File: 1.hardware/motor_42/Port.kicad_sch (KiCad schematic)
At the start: 0 parts

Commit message: 중간 저장
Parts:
- added J1, J2: Conn_01x06, symbol Connector_Generic:Conn_01x06
- added R11: 120/0.1w, symbol Device:R_Small_US
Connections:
- new net CAN_H: R11.2
- new net GND: J1.5 (Pin_5), J1.6 (Pin_6), J2.5 (Pin_5), J2.6 (Pin_6)
- new net VCC_IN: J1.1 (Pin_1), J1.2 (Pin_2), J2.1 (Pin_1), J2.2 (Pin_2)

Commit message: 살짝 변경
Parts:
- added J3: Conn_01x03, symbol Connector_Generic:Conn_01x03
- added JP2: SolderJumper_2_Open, Jumper:SolderJumper-2_P1.3mm_Open_RoundedPad1.0x1.5mm, symbol Jumper:SolderJumper_2_Open
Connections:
- net CAN_H: now also J1.3 (Pin_3), J2.3 (Pin_3)
- net CAN_L: now also J1.4 (Pin_4), J2.4 (Pin_4), JP2.2 (B)
- net at R11.1: now also JP2.1 (A)

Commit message: 중간 저장
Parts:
- added J4: Conn_01x05, symbol Connector_Generic:Conn_01x05
- added J5: Conn_01x06, symbol Connector_Generic:Conn_01x06
- added SW1, SW2: SW_Push, symbol Switch:SW_Push
- added U5: SN65HVD232, Package_SO:SOIC-8_3.9x4.9mm_P1.27mm, symbol Interface_CAN_LIN:SN65HVD232
- J1: value Conn_01x06 -> CAN_IN
- J2: value Conn_01x06 -> CAN_OUT
- J3: value Conn_01x03 -> DEBUG
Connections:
- net CAN_H: now also U5.7 (CANH)
- net CAN_L: now also U5.6 (CANL)
- net GND: now also J3.3 (Pin_3), J4.3 (Pin_3), J5.2 (Pin_2), SW1.2, SW2.2, U5.2 (GND)
- net SWDIO: now reaches J3.1 (Pin_1)
- net SWCLK: now reaches J3.2 (Pin_2)
- new net 3V3: J5.1 (Pin_1), U5.3 (VCC)
- new net ADC_ENC: J4.5 (Pin_5)
- new net ADC_VREF_2V5: J4.4 (Pin_4)
- new net BTN1: SW1.1
- new net BTN2: SW2.1
- new net CAN_RX: U5.4 (R)
- new net CAN_TX: U5.1 (D)
- new net MT6816_CSN: J5.6 (Pin_6)
- new net SPI1_CLK: J5.3 (Pin_3)
- new net SPI1_MISO: J5.5 (Pin_5)
- new net SPI1_MOSI: J5.4 (Pin_4)
- new net UART1_RX: J4.1 (Pin_1)
- new net UART1_TX: J4.2 (Pin_2)
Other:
- moved on the sheet: J3, JP2, R11

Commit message: 중간 저장
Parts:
- added J6: Conn_01x03, symbol Connector_Generic:Conn_01x03
- SW1, SW2: footprint (none) -> mylib:TSB008A2530A
- renumbered J4 to J1, J3 to J2, J1 to J3, J2 to J4, JP2 to JP1, R11 to R18, U5 to U3
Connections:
- net GND: now also J6.3 (Pin_3)
- new net ESP_RX0: J6.1 (Pin_1)
- new net ESP_TX0: J6.2 (Pin_2)
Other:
- moved on the sheet: J1, J2, J3, J4, J5, JP1, R18, SW1, SW2, U3

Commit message: 회로도 대충 완성
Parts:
- removed SW1, SW2: SW_Push, mylib:TSB008A2530A, symbol Switch:SW_Push
- added D4: PRTR5V0U2X, Package_TO_SOT_SMD:SOT-143, symbol Power_Protection:PRTR5V0U2X
- added J11, J12: Conn_01x02, symbol Connector_Generic:Conn_01x02
- added J3: USB_C, Connector_USB:USB_C_Receptacle_HRO_TYPE-C-31-M-12, symbol USB-C-USB-2.0-cache:Connector_USB_C_Receptacle_USB2.0
- added J9: DEBUG, symbol Connector_Generic:Conn_01x03
- added JP2, JP3, JP4, JP5: SolderJumper_3_Bridged123, Jumper:SolderJumper-3_P1.3mm_Bridged123_RoundedPad1.0x1.5mm, symbol Jumper:SolderJumper_3_Bridged123
- added R24: NC_4.7K, Resistor_SMD:R_0402_1005Metric, symbol Device:R_Small_US
- added R25: 4.7K, Resistor_SMD:R_0402_1005Metric, symbol Device:R_Small_US
- added R39: 4.7k/0.063w, Resistor_SMD:R_0402_1005Metric, symbol Device:R_Small_US
- renumbered J5 to J2, J2 to J4, J3 to J5, J4 to J6, J6 to J7, R18 to R26
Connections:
- net GND: now also D4.1 (GND), J3.A1 (GND), J3.A12 (GND), J3.B1 (GND), J3.B12 (GND), J3.S1 (SHIELD), J9.3 (Pin_3), R25.2
- new net: J3.A5 (CC1), J3.B5 (CC2), R24.2, R25.1
- new net 5V: J9.1 (Pin_1), R39.1
- new net OUT_A+: J11.1 (Pin_1), JP2.1 (A), JP2.2 (C), JP2.3 (B)
- new net OUT_A-: J11.2 (Pin_2), JP3.1 (A), JP3.2 (C), JP3.3 (B)
- new net OUT_B+: J12.1 (Pin_1), JP4.1 (A), JP4.2 (C), JP4.3 (B)
- new net OUT_B-: J12.2 (Pin_2), JP5.1 (A), JP5.2 (C), JP5.3 (B)
- new net USB_DM: D4.3 (I/O2), J3.A7 (D-), J3.B7 (D-)
- new net USB_DP: D4.2 (I/O1), J3.A6 (D+), J3.B6 (D+)
- new net VBUS: D4.4 (VCC), J3.A4 (VBUS), J3.A9 (VBUS), J3.B4 (VBUS), J3.B9 (VBUS), R24.1
- new net WS2812_SIGNAL: J9.2 (Pin_2), R39.2
- no-connect marks 0 -> 2
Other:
- note added: "USB"

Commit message: 수정
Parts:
- J1: value Conn_01x05 -> PC_CONN; footprint (none) -> Connector_JST:JST_SH_SM05B-SRSS-TB_1x05-1MP_P1.00mm_Horizontal
- J11, J12: value Conn_01x02 -> WAGO_2060
- J2: value Conn_01x06 -> MT6816_CONN; footprint (none) -> Connector_JST:JST_SH_SM05B-SRSS-TB_1x05-1MP_P1.00mm_Horizontal
- J4: footprint (none) -> Connector_JST:JST_SH_SM03B-SRSS-TB_1x03-1MP_P1.00mm_Horizontal
- J5, J6: footprint (none) -> Connector_JST:JST_SH_SM06B-SRSS-TB_1x06-1MP_P1.00mm_Horizontal
- J7: value Conn_01x03 -> ESP_DOWNLOAD; footprint (none) -> Connector_JST:JST_SH_SM03B-SRSS-TB_1x03-1MP_P1.00mm_Horizontal
- J9: value DEBUG -> WS2812_OUT; footprint (none) -> Connector_JST:JST_SH_SM03B-SRSS-TB_1x03-1MP_P1.00mm_Horizontal
- JP1: value SolderJumper_2_Open -> CAN_END_PAD
- JP2: value SolderJumper_3_Bridged123 -> PAD_OUTA_P
- JP3: value SolderJumper_3_Bridged123 -> PAD_OUTA_M
- JP4: value SolderJumper_3_Bridged123 -> PAD_OUTB_P
- JP5: value SolderJumper_3_Bridged123 -> PAD_OUTB_M
- R26: footprint (none) -> Resistor_SMD:R_0603_1608Metric
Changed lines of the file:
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@@
 			)
 		)
-		(property "Footprint" ""
+		(property "Footprint" "Connector_JST:JST_SH_SM06B-SRSS-TB_1x06-1MP_P1.00mm_Horizontal"
 			(at 72.39 50.8 0)
 			(effects
@@
 			)
 		)
-		(property "Value" "Conn_01x06"
+		(property "Value" "MT6816_CONN"
 			(at 33.02 69.85 0)
 			(effects
@@
 			)
 		)
-		(property "Footprint" ""
+		(property "Footprint" "Connector_JST:JST_SH_SM05B-SRSS-TB_1x05-1MP_P1.00mm_Horizontal"
 			(at 33.02 58.42 0)
 			(effects
@@
 			)
 		)
-		(property "Value" "DEBUG"
+		(property "Value" "WS2812_OUT"
 			(at 105.41 35.56 0)
 			(effects
@@
 			)
 		)
-		(property "Footprint" ""
+		(property "Footprint" "Connector_JST:JST_SH_SM03B-SRSS-TB_1x03-1MP_P1.00mm_Horizontal"
 			(at 105.41 29.21 0)
 			(effects
@@
 		(fields_autoplaced yes)
 		(property "Reference" "J7"
-			(at 137.16 49.5299 0)
-			(effects
-				(font
-					(size 1.27 1.27)
-				)
-				(justify left)
-			)
-		)
-		(property "Value" "Conn_01x03"
-			(at 137.16 52.0699 0)
-			(effects
-				(font
-					(size 1.27 1.27)
-				)
-				(justify left)
-			)
-		)
-		(property "Footprint" ""
+			(at 139.7 41.91 0)
+			(effects
+				(font
+					(size 1.27 1.27)
+				)
+			)
+		)
+		(property "Value" "ESP_DOWNLOAD"
+			(at 139.7 44.45 0)
+			(effects
+				(font
+					(size 1.27 1.27)
+				)
+			)
+		)
+		(property "Footprint" "Connector_JST:JST_SH_SM03B-SRSS-TB_1x03-1MP_P1.00mm_Horizontal"
 			(at 139.7 50.8 0)
 			(effects
@@
 			)
 		)
-		(property "Value" "SolderJumper_3_Bridged123"
+		(property "Value" "PAD_OUTA_P"
 			(at 175.26 63.5 0)
 			(effects
@@
 			)
 		)
-		(property "Value" "SolderJumper_2_Open"
+		(property "Value" "CAN_END_PAD"
 			(at 100.33 76.2 0)
 			(effects
@@
 			)
 		)
-		(property "Value" "Conn_01x02"
+		(property "Value" "WAGO_2060"
 			(at 139.7 95.25 0)
 			(effects
@@
 			)
 		)
-		(property "Value" "SolderJumper_3_Bridged123"
+		(property "Value" "PAD_OUTB_P"
 			(at 175.26 87.63 0)
 			(effects
@@
 			)
 		)
-		(property "Value" "SolderJumper_3_Bridged123"
+		(property "Value" "PAD_OUTB_M"
 			(at 175.26 99.06 0)
 			(effects
@@
 			)
 		)
-		(property "Footprint" ""
+		(property "Footprint" "Resistor_SMD:R_0603_1608Metric"
 			(at 91.44 80.01 0)
 			(effects
@@
 			)
 		)
-		(property "Value" "Conn_01x02"
+		(property "Value" "WAGO_2060"
 			(at 139.7 77.47 0)
 			(effects
@@
 			)
 		)
-		(property "Value" "SolderJumper_3_Bridged123"
+		(property "Value" "PAD_OUTA_M"
 			(at 175.26 76.2 0)
 			(effects
@@
 			)
 		)
-		(property "Value" "Conn_01x05"
+		(property "Value" "PC_CONN"
 			(at 33.02 36.83 0)
 			(effects
@@
 			)
 		)
-		(property "Footprint" ""
+		(property "Footprint" "Connector_JST:JST_SH_SM05B-SRSS-TB_1x05-1MP_P1.00mm_Horizontal"
 			(at 33.02 27.94 0)
 			(effects
@@
 			)
 		)
-		(property "Footprint" ""
+		(property "Footprint" "Connector_JST:JST_SH_SM06B-SRSS-TB_1x06-1MP_P1.00mm_Horizontal"
 			(at 105.41 50.8 0)
 			(effects
@@
 			)
 		)
-		(property "Footprint" ""
+		(property "Footprint" "Connector_JST:JST_SH_SM03B-SRSS-TB_1x03-1MP_P1.00mm_Horizontal"
 			(at 72.39 29.21 0)
 			(effects

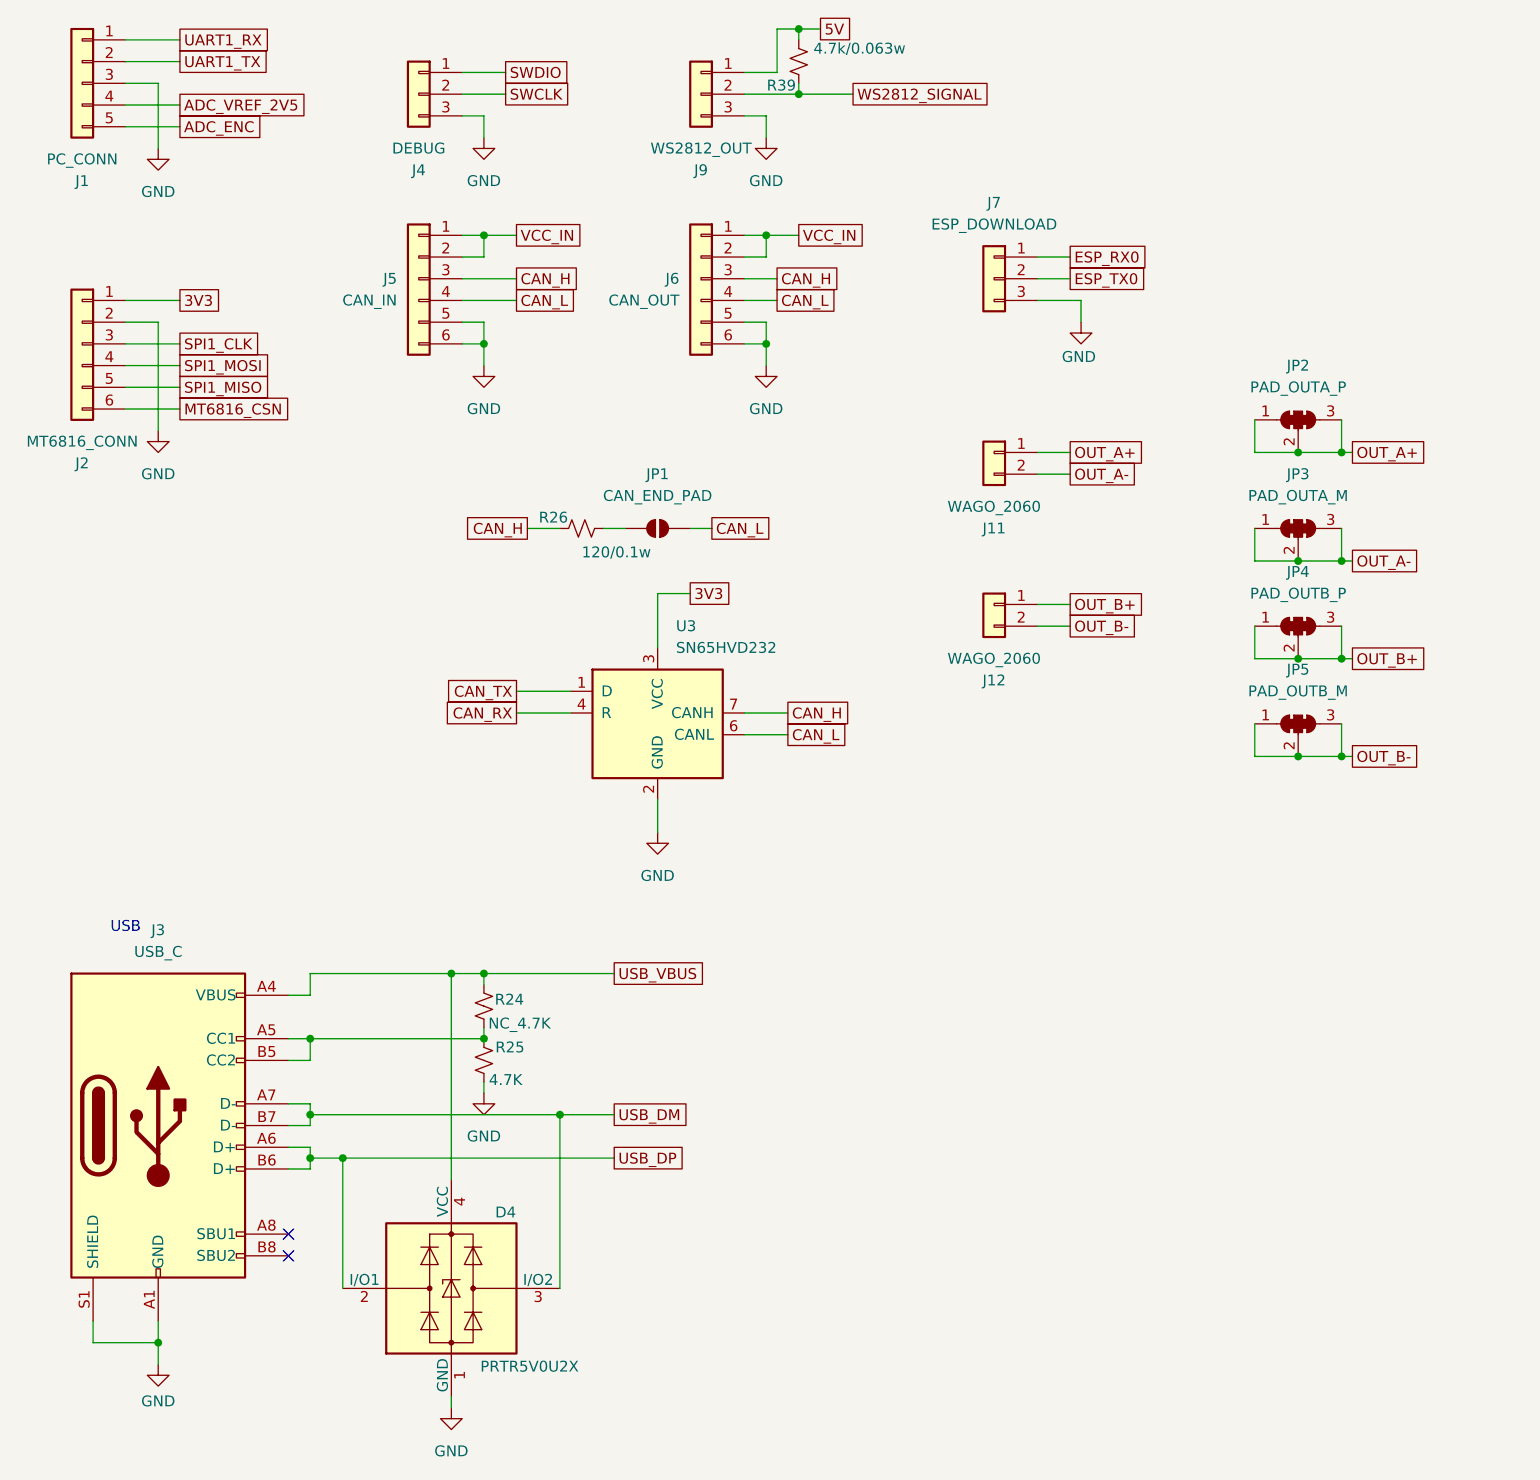
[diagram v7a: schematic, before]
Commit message: 3V3 LDO변경 및 대략적 위치 세팅
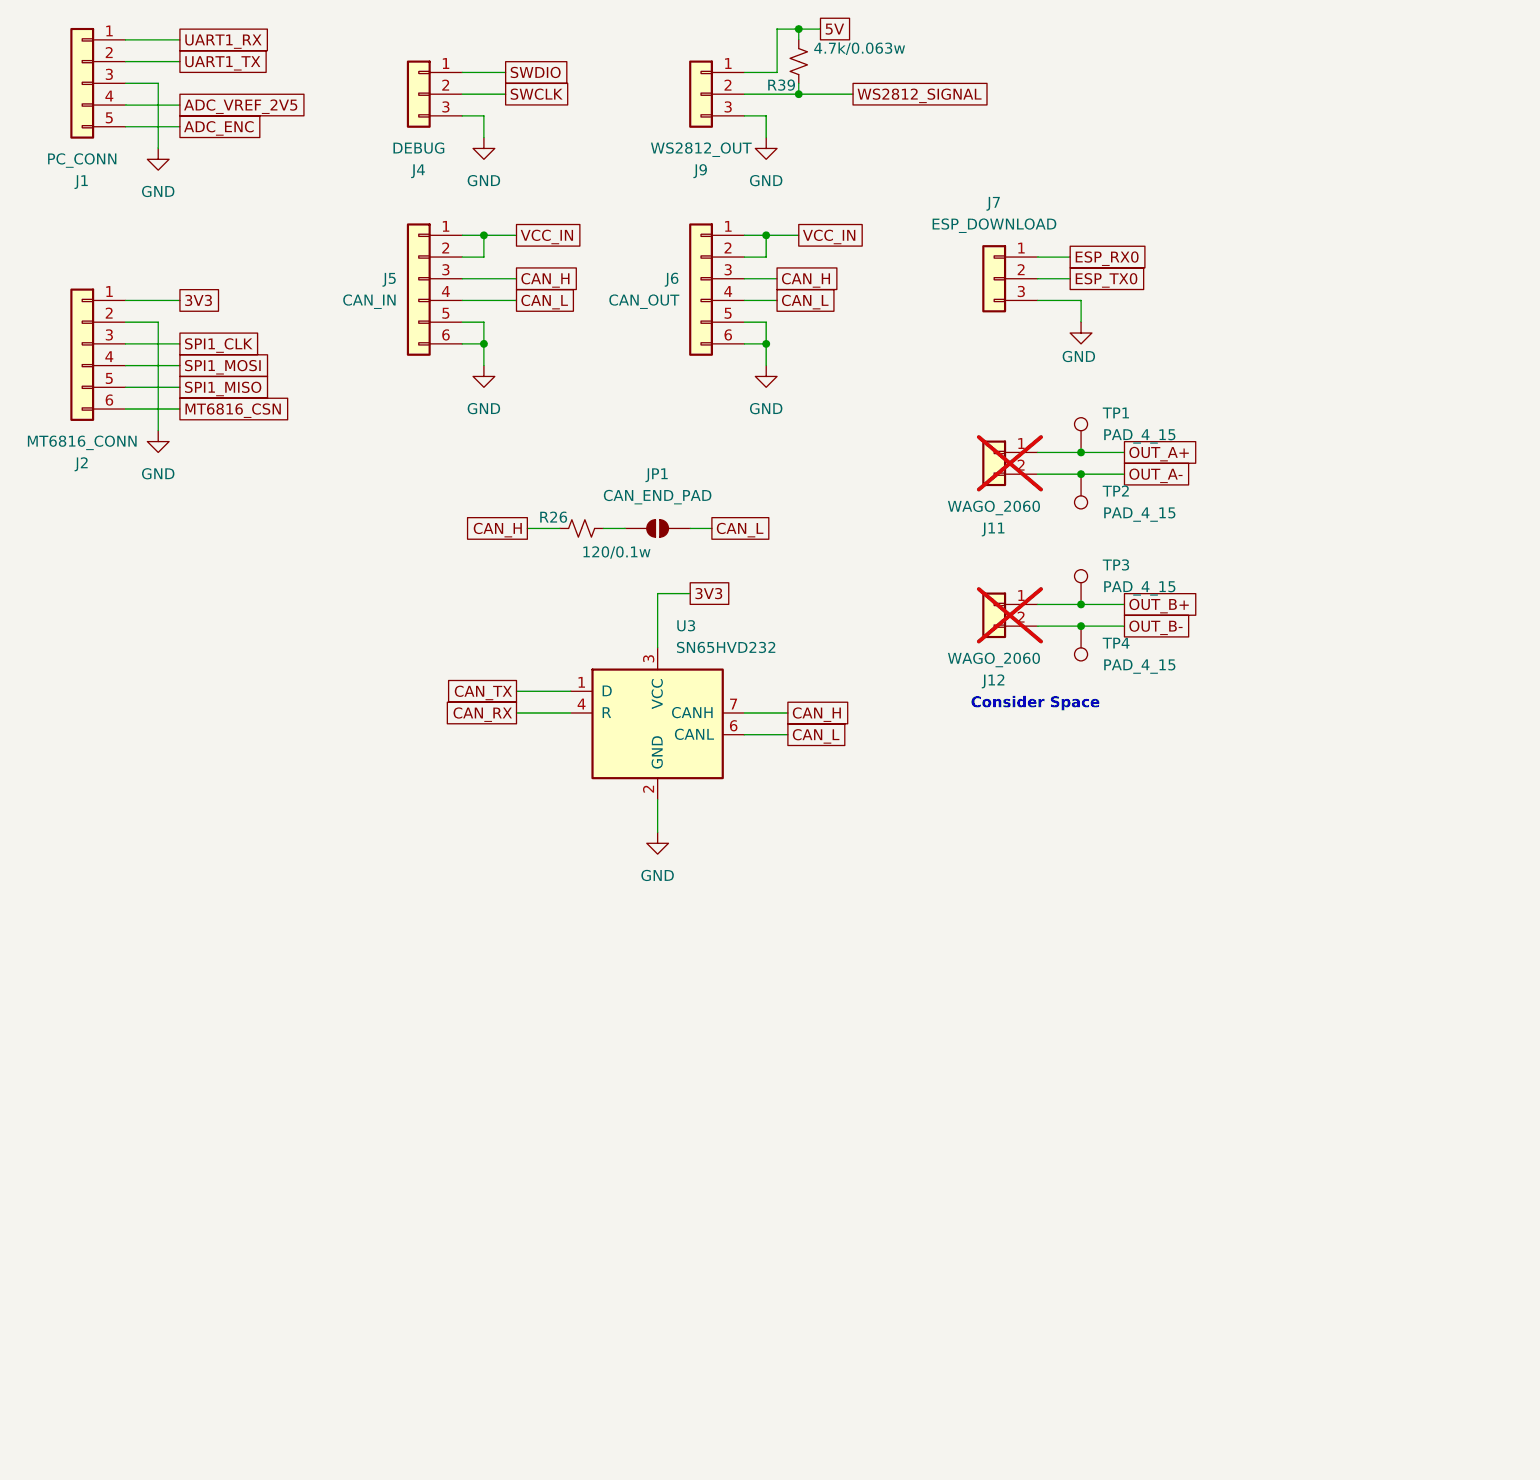
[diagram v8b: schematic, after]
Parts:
- removed D4: PRTR5V0U2X, Package_TO_SOT_SMD:SOT-143, symbol Power_Protection:PRTR5V0U2X
- removed J3: USB_C, Connector_USB:USB_C_Receptacle_HRO_TYPE-C-31-M-12, symbol USB-C-USB-2.0-cache:Connector_USB_C_Receptacle_USB2.0
- removed JP2: PAD_OUTA_P, Jumper:SolderJumper-3_P1.3mm_Bridged123_RoundedPad1.0x1.5mm, symbol Jumper:SolderJumper_3_Bridged123
- removed JP3: PAD_OUTA_M, Jumper:SolderJumper-3_P1.3mm_Bridged123_RoundedPad1.0x1.5mm, symbol Jumper:SolderJumper_3_Bridged123
- removed JP4: PAD_OUTB_P, Jumper:SolderJumper-3_P1.3mm_Bridged123_RoundedPad1.0x1.5mm, symbol Jumper:SolderJumper_3_Bridged123
- removed JP5: PAD_OUTB_M, Jumper:SolderJumper-3_P1.3mm_Bridged123_RoundedPad1.0x1.5mm, symbol Jumper:SolderJumper_3_Bridged123
- removed R24: NC_4.7K, Resistor_SMD:R_0402_1005Metric, symbol Device:R_Small_US
- removed R25: 4.7K, Resistor_SMD:R_0402_1005Metric, symbol Device:R_Small_US
- added TP1, TP2, TP3, TP4: PAD_4_15, New_Footprints:custom_pad_4_15, symbol Connector:TestPoint
- J11, J12: now not fitted; now left out of the parts list
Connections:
- net OUT_A+: now also TP1.1
- net OUT_A-: now also TP2.1
- net OUT_B+: now also TP3.1
- net OUT_B-: now also TP4.1
- no-connect marks 2 -> 0
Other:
- note added: "Consider Space"
- note removed: "USB"
